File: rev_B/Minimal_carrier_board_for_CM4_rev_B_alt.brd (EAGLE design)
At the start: 71.1 x 63.5 mm, 23 parts, among them IC1 MC74VHC1G14DFT1G, J1 P1-100, J2 P101-200, J5 HRO_31_M_12_USB_C, J6 629104190121, J7 SFW15R-2STE1LF

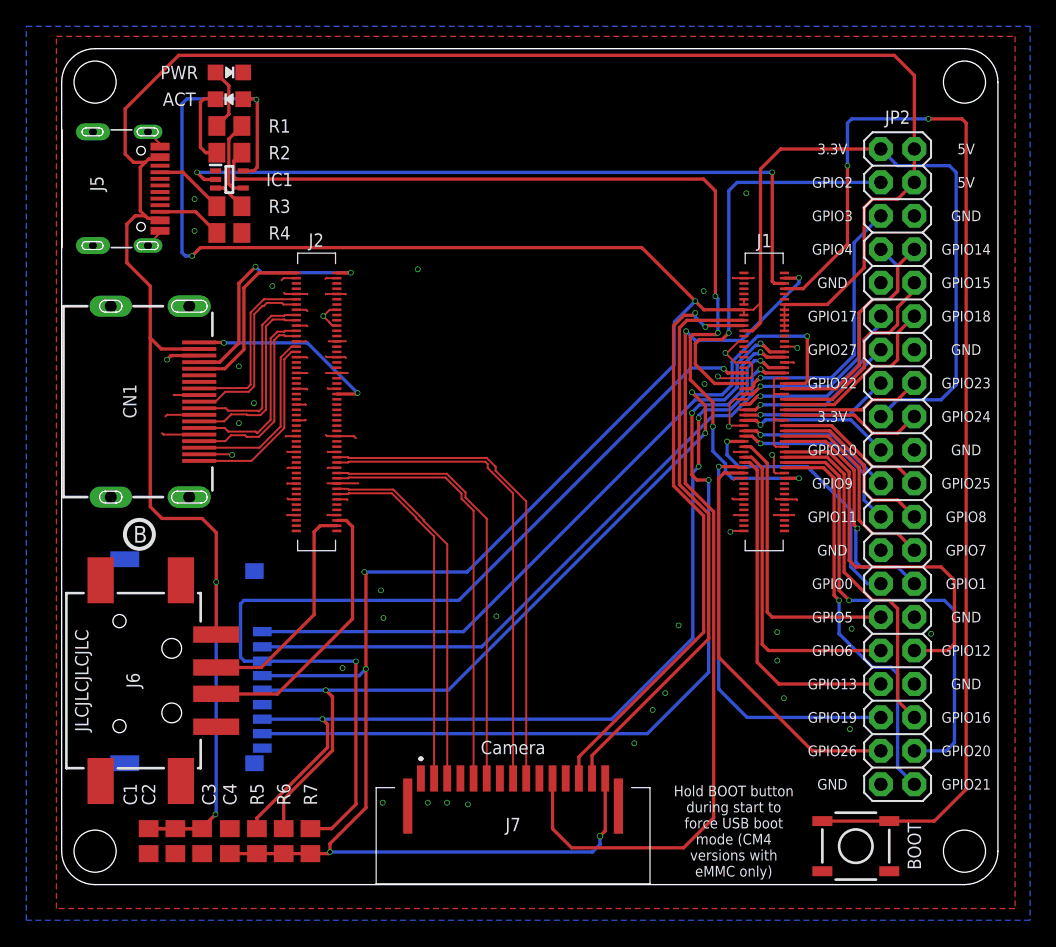
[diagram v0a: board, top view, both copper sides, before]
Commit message: Update
- renamed files so there are now 2 versions of rev.B:

rev.B now have 15-pin connector for RPi camera  module
rev.B_alt have 22-pin connector for RPi camera module and DSI display
- added/updated pictures for both versions of the board
- updated README accordingly
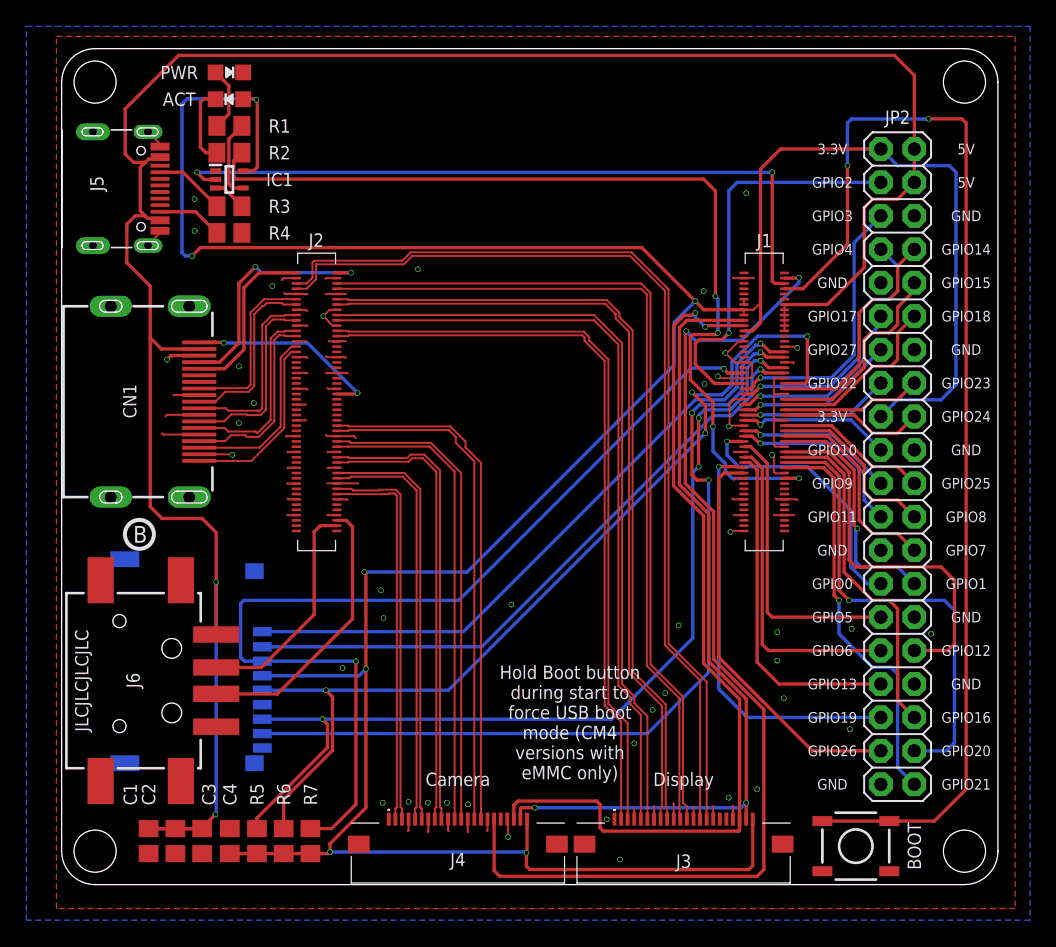
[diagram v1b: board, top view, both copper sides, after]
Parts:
- removed J7: SFW15R-2STE1LF, SamacSys_Parts:SFW15R2STE1LF
- added J3, J4: 54548-2271, dronecz:545482271
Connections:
- new net N$24: J3.17
- new net N$25: J3.18
- net 3.3V: now also J3.22, J4.22; no longer J7.15
- net CAM1_C_N: now also J4.8; no longer J7.8
- net CAM1_C_P: now also J4.9; no longer J7.9
- net CAM1_D0_N: now also J4.2; no longer J7.2
- net CAM1_D0_P: now also J4.3; no longer J7.3
- net CAM1_D1_N: now also J4.5; no longer J7.5
- net CAM1_D1_P: now also J4.6; no longer J7.6
- net CAM1_D2_N: now also J4.11
- net CAM1_D2_P: now also J4.12
- net CAM1_D3_N: now also J4.14
- net CAM1_D3_P: now also J4.15
- net CAM_GPIO: now also J4.17; no longer J7.11
- net DSI1_C_N: now also J3.8
- net DSI1_C_P: now also J3.9
- net DSI1_D0_N: now also J3.2
- net DSI1_D0_P: now also J3.3
- net DSI1_D1_N: now also J3.5
- net DSI1_D1_P: now also J3.6
- net DSI1_D2_N: now also J3.11
- net DSI1_D2_P: now also J3.12
- net DSI1_D3_N: now also J3.14
- net DSI1_D3_P: now also J3.15
- net GND: now also J3.1, J3.10, J3.13, J3.16, J3.19, J3.4, J3.7, J4.1, J4.10, J4.13, J4.16, J4.19, J4.4, J4.7; no longer J7.1, J7.10, J7.4, J7.7
- net SCL0: now also J3.20, J4.20; no longer J7.13
- net SDA0: now also J3.21, J4.21; no longer J7.14
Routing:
- net DSI1_D3_P: track 0.00 -> 72.5 mm
- net DSI1_D3_N: track 0.00 -> 72.0 mm
- net DSI1_D2_P: track 0.00 -> 65.2 mm
- net DSI1_D2_N: track 0.00 -> 64.6 mm
- net DSI1_C_P: track 0.00 -> 61.9 mm
- net DSI1_C_N: track 0.00 -> 61.4 mm
- net DSI1_D1_P: track 0.00 -> 59.5 mm
- net DSI1_D1_N: track 0.00 -> 58.9 mm
- net DSI1_D0_P: track 0.00 -> 57.2 mm
- net DSI1_D0_N: track 0.00 -> 56.6 mm
- net CAM1_D3_P: track 0.00 -> 39.4 mm
- net CAM1_D3_N: track 0.00 -> 38.9 mm
- net CAM1_D2_P: track 0.00 -> 36.7 mm
- net CAM1_D2_N: track 0.00 -> 36.1 mm
- net SCL0: track 45.7 -> 67.2 mm
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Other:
- board text added: "Display"
- board text added: "Hold Boot button during start to force USB boot mode (CM4 versions with eMMC only)"
- board text removed: "Hold BOOT button during start to force USB boot mode (CM4 versions with eMMC only)"
